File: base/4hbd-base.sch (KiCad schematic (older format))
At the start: 13 parts, among them J1 Screw_Terminal_01x03, J10 Screw_Terminal_01x04, J11 Screw_Terminal_01x02, J12 Conn_01x03, J13 Conn_01x08, J2 Screw_Terminal_01x03, J3 Screw_Terminal_01x03, J4 Screw_Terminal_01x03, J5 Screw_Terminal_01x02, J6 Screw_Terminal_01x02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

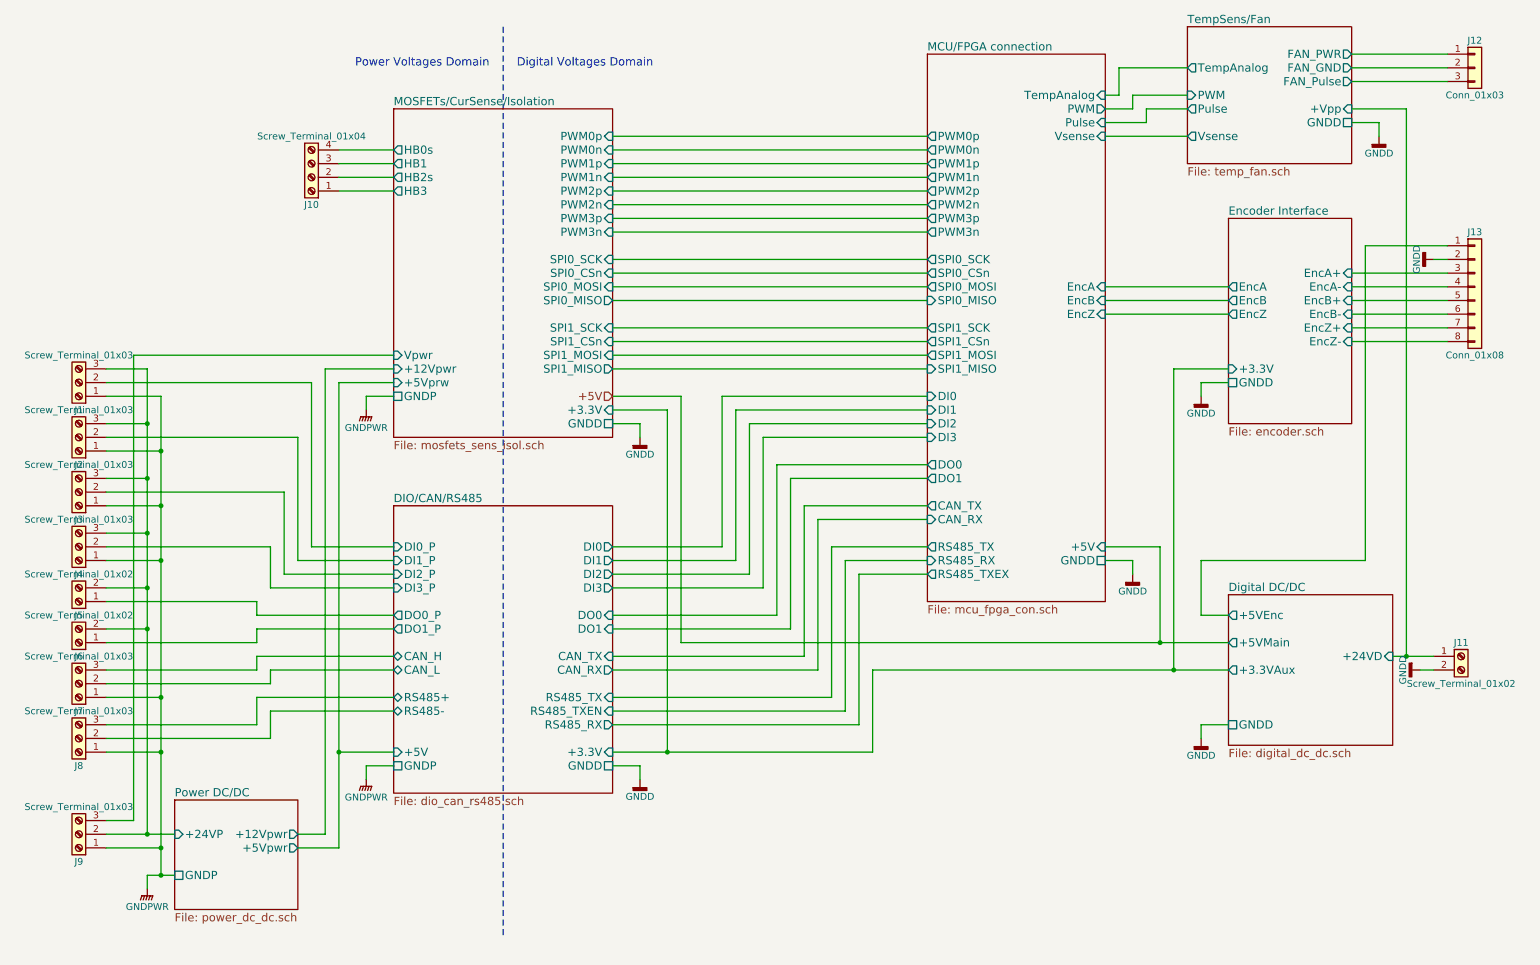
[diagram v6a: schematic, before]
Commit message: 1. Separate dio_can_rs485 sheet into two: dio + can_rs485. 2. Move can and rs485 into digital power domain 3. Add CAN transiever to can_rs485 sheet
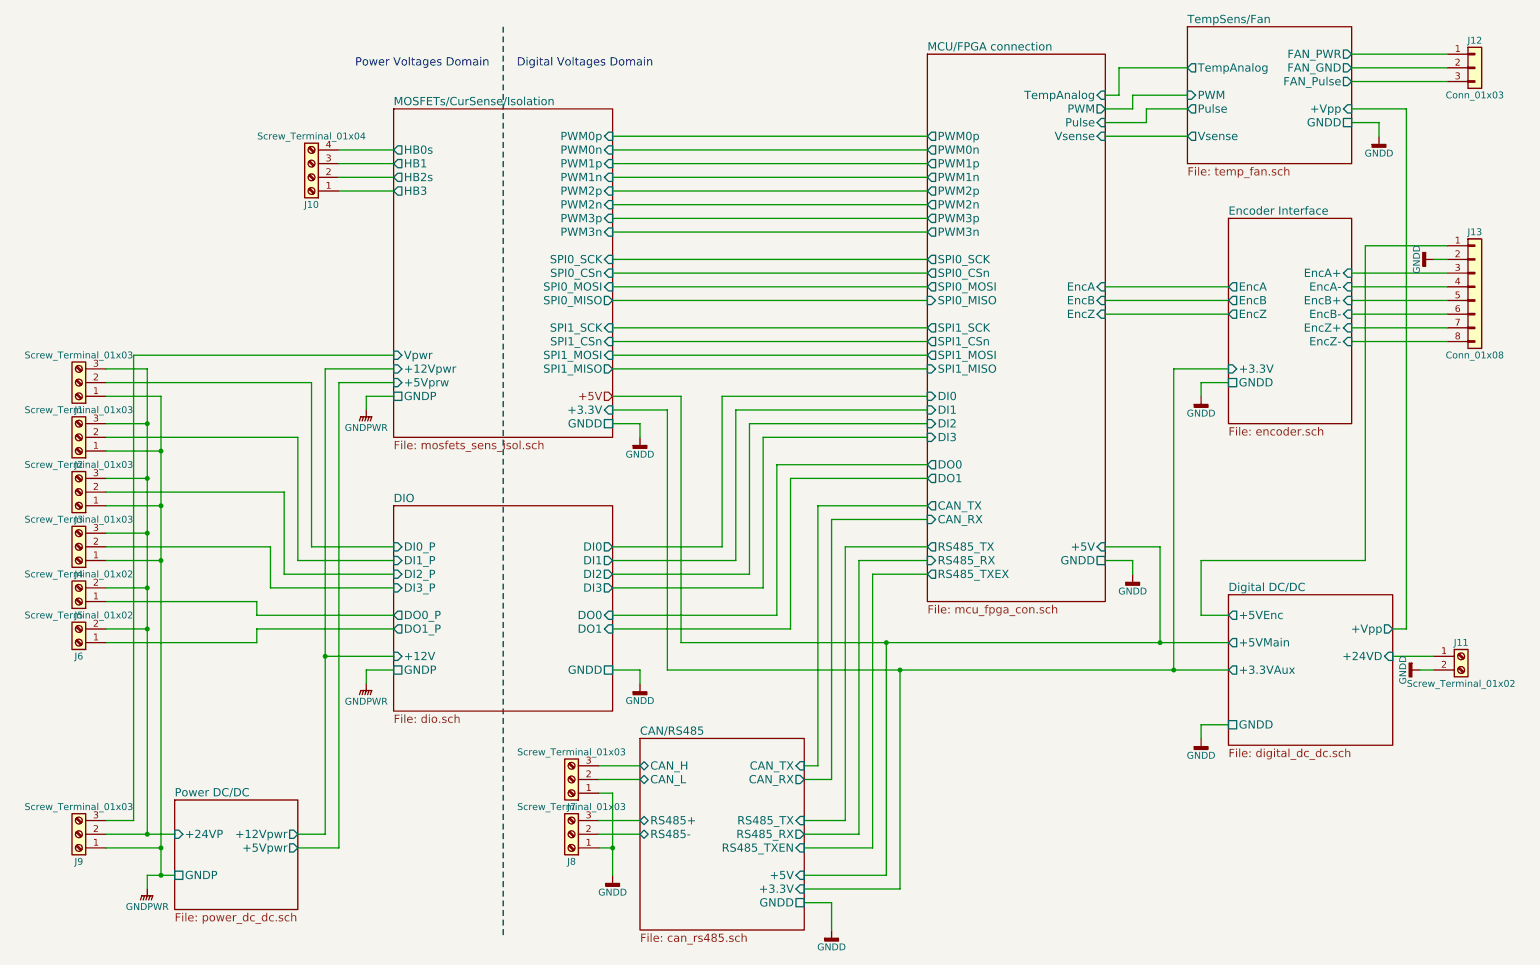
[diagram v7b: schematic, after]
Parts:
- J13: footprint (none) -> Connector_PinHeader_2.54mm:PinHeader_1x08_P2.54mm_Horizontal
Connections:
- net GNDD: now also J7.1 (Pin_1), J8.1 (Pin_1)
- net GNDPWR: no longer J7.1 (Pin_1), J8.1 (Pin_1)
- net DIO/CAN/RS485/CAN_H renamed CAN/RS485/CAN_H
- net DIO/CAN/RS485/CAN_L renamed CAN/RS485/CAN_L
- net DIO/CAN/RS485/DI0_P renamed DIO/DI0_P
- net DIO/CAN/RS485/DI1_P renamed DIO/DI1_P
- net DIO/CAN/RS485/DI2_P renamed DIO/DI2_P
- net DIO/CAN/RS485/DI3_P renamed DIO/DI3_P
- net DIO/CAN/RS485/DO0_P renamed DIO/DO0_P
- net DIO/CAN/RS485/DO1_P renamed DIO/DO1_P
- net DIO/CAN/RS485/RS485+ renamed CAN/RS485/RS485+
- net DIO/CAN/RS485/RS485- renamed CAN/RS485/RS485-
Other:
- moved on the sheet: J7, J8
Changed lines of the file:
@@
 LIBS:dc-dc
 LIBS:regul
+LIBS:interface
+LIBS:ESD_Protection
 LIBS:4hbd-base-cache
 EELAYER 25 0
@@
 $Descr A4 11693 8268
 encoding utf-8
-Sheet 1 8
+Sheet 1 9
 Title ""
 Date ""
@@
 $EndSheet
 $Sheet
-S 3000 4300 1600 2100
+S 3000 4300 1600 1500
 U 5A1BA75E
-F0 "DIO/CAN/RS485" 60
-F1 "dio_can_rs485.sch" 60
+F0 "DIO" 60
+F1 "dio.sch" 60
 F2 "DI0_P" I L 3000 4600 60
 F3 "DI1_P" I L 3000 4700 60
@@
 F6 "DO0_P" O L 3000 5100 60
 F7 "DO1_P" O L 3000 5200 60
-F8 "CAN_H" B L 3000 5400 60
-F9 "CAN_L" B L 3000 5500 60
-F10 "DI0" O R 4600 4600 60
-F11 "DI1" O R 4600 4700 60
-F12 "DI2" O R 4600 4800 60
-F13 "DI3" O R 4600 4900 60
-F14 "DO0" I R 4600 5100 60
-F15 "DO1" I R 4600 5200 60
-F16 "CAN_TX" I R 4600 5400 60
-F17 "CAN_RX" O R 4600 5500 60
-F18 "RS485_TX" I R 4600 5700 60
-F19 "RS485_TXEN" I R 4600 5800 60
-F20 "RS485_RX" O R 4600 5900 60
-F21 "RS485+" B L 3000 5700 60
-F22 "RS485-" B L 3000 5800 60
-F23 "+3.3V" I R 4600 6100 60
-F24 "GNDD" U R 4600 6200 60
-F25 "+5V" I L 3000 6100 60
-F26 "GNDP" U L 3000 6200 60
+F8 "DI0" O R 4600 4600 60
+F9 "DI1" O R 4600 4700 60
+F10 "DI2" O R 4600 4800 60
+F11 "DI3" O R 4600 4900 60
+F12 "DO0" I R 4600 5100 60
+F13 "DO1" I R 4600 5200 60
+F14 "GNDD" U R 4600 5500 60
+F15 "GNDP" U L 3000 5500 60
+F16 "+12V" I L 3000 5400 60
 $EndSheet
 Text Notes 3700 1100 2    60   ~ 0
@@
 F5 "+3.3VAux" O L 9100 5500 60
 F6 "GNDD" U L 9100 5900 60
+F7 "+Vpp" O R 10300 5200 60
 $EndSheet
 $Sheet
@@
 L GNDD #PWR5
 U 1 1 5A1C5445
-P 4800 6300
-F 0 "#PWR5" H 4800 6050 50  0001 C CNN
-F 1 "GNDD" H 4800 6175 50  0000 C CNN
-F 2 "" H 4800 6300 50  0001 C CNN
-F 3 "" H 4800 6300 50  0001 C CNN
-	1    4800 6300
+P 4800 5600
+F 0 "#PWR5" H 4800 5350 50  0001 C CNN
+F 1 "GNDD" H 4800 5475 50  0000 C CNN
+F 2 "" H 4800 5600 50  0001 C CNN
+F 3 "" H 4800 5600 50  0001 C CNN
+	1    4800 5600
 	1    0    0    -1
 $EndComp
@@
 F 0 "J13" H 10900 3100 50  0000 C CNN
 F 1 "Conn_01x08" H 10900 2200 50  0000 C CNN
-F 2 "" H 10900 2700 50  0001 C CNN
+F 2 "Connector_PinHeader_2.54mm:PinHeader_1x08_P2.54mm_Horizontal" H 10900 2700 50  0001 C CNN
 F 3 "" H 10900 2700 50  0001 C CNN
 	1    10900 2700
@@
 	8900 3400 8900 3500
 Wire Wire Line
-	4600 6200 4800 6200
-Wire Wire Line
-	4800 6200 4800 6300
+	4600 5500 4800 5500
+Wire Wire Line
+	4800 5500 4800 5600
 Wire Wire Line
 	4600 3700 4800 3700
@@
 	5900 5200 4600 5200
 Wire Wire Line
-	4600 5400 6000 5400
-Wire Wire Line
-	6000 5400 6000 4300
-Wire Wire Line
-	6100 4400 6100 5500
-Wire Wire Line
-	6100 5500 4600 5500
-Wire Wire Line
-	4600 5700 6200 5700
-Wire Wire Line
-	6200 5700 6200 4600
-Wire Wire Line
-	6300 4700 6300 5800
-Wire Wire Line
-	6300 5800 4600 5800
-Wire Wire Line
-	4600 5900 6400 5900
-Wire Wire Line
-	6400 5900 6400 4800
-Wire Wire Line
-	6500 6100 6500 5500
-Wire Wire Line
-	4600 6100 6500 6100
-Wire Wire Line
 	4600 3600 5000 3600
-Wire Wire Line
-	5000 3600 5000 6100
-Connection ~ 5000 6100
 Wire Wire Line
 	8700 5500 8700 3300
@@
 	5900 4100 6900 4100
 Wire Wire Line
-	6500 5500 9100 5500
-Wire Wire Line
-	6000 4300 6900 4300
-Wire Wire Line
-	6100 4400 6900 4400
-Wire Wire Line
-	6200 4600 6900 4600
-Wire Wire Line
-	6300 4700 6900 4700
-Wire Wire Line
-	6400 4800 6900 4800
+	5000 5500 9100 5500
 Wire Wire Line
 	4600 2800 6900 2800
@@
 	8900 4700 10100 4700
 Wire Wire Line
-	10400 1400 10400 5400
-Wire Wire Line
 	10400 1400 10000 1400
-Connection ~ 10400 5400
 $Comp
 L Conn_01x03 J12
@@
 	2800 3500 2800 3600
 Wire Wire Line
-	3000 6200 2800 6200
-Wire Wire Line
-	2800 6200 2800 6300
+	3000 5500 2800 5500
+Wire Wire Line
+	2800 5500 2800 5600
 Wire Wire Line
 	1200 7000 1400 7000
@@
 L GNDPWR #PWR3
 U 1 1 5A1F43A1
-P 2800 6300
-F 0 "#PWR3" H 2800 6100 50  0001 C CNN
-F 1 "GNDPWR" H 2800 6170 50  0000 C CNN
-F 2 "" H 2800 6250 50  0001 C CNN
-F 3 "" H 2800 6250 50  0001 C CNN
-	1    2800 6300
+P 2800 5600
+F 0 "#PWR3" H 2800 5400 50  0001 C CNN
+F 1 "GNDPWR" H 2800 5470 50  0000 C CNN
+F 2 "" H 2800 5550 50  0001 C CNN
+F 3 "" H 2800 5550 50  0001 C CNN
+	1    2800 5600
 	1    0    0    -1
 $EndComp
@@
 	2600 3400 2600 6800
 Wire Wire Line
-	2600 6100 3000 6100
-Wire Wire Line
 	2600 3400 3000 3400
-Connection ~ 2600 6100
 Wire Wire Line
 	2300 6700 2500 6700
@@
 L Screw_Terminal_01x03 J8
 U 1 1 5A1F99A1
-P 700 6000
-F 0 "J8" H 700 6200 50  0000 C CNN
-F 1 "Screw_Terminal_01x03" H 700 5800 50  0000 C CNN
-F 2 "" H 700 6000 50  0001 C CNN
-F 3 "" H 700 6000 50  0001 C CNN
-	1    700  6000
+P 4300 6700
+F 0 "J8" H 4300 6900 50  0000 C CNN
+F 1 "Screw_Terminal_01x03" H 4300 6500 50  0000 C CNN
+F 2 "" H 4300 6700 50  0001 C CNN
+F 3 "" H 4300 6700 50  0001 C CNN
+	1    4300 6700
 	-1   0    0    1
 $EndComp
@@
 L Screw_Terminal_01x03 J7
 U 1 1 5A1F9CC3
-P 700 5600
-F 0 "J7" H 700 5800 50  0000 C CNN
-F 1 "Screw_Terminal_01x03" H 700 5400 50  0000 C CNN
-F 2 "" H 700 5600 50  0001 C CNN
-F 3 "" H 700 5600 50  0001 C CNN
-	1    700  5600
+P 4300 6300
+F 0 "J7" H 4300 6500 50  0000 C CNN
+F 1 "Screw_Terminal_01x03" H 4300 6100 50  0000 C CNN
+F 2 "" H 4300 6300 50  0001 C CNN
+F 3 "" H 4300 6300 50  0001 C CNN
+	1    4300 6300
 	-1   0    0    1
 $EndComp
@@
 	1300 3500 1300 7000
 Connection ~ 1300 7000
-Wire Wire Line
-	1300 6100 900  6100
 Connection ~ 1300 6800
-Wire Wire Line
-	1300 5700 900  5700
-Connection ~ 1300 6100
 Wire Wire Line
 	1200 3300 1200 6700
@@
 Wire Wire Line
 	1300 4700 900  4700
-Connection ~ 1300 5700
 Wire Wire Line
 	1300 4300 900  4300
@@
 Wire Wire Line
 	2000 5300 900  5300
-Wire Wire Line
-	3000 5400 2000 5400
-Wire Wire Line
-	2000 5400 2000 5500
-Wire Wire Line
-	2000 5500 900  5500
-Wire Wire Line
-	3000 5500 2100 5500
-Wire Wire Line
-	2100 5500 2100 5600
-Wire Wire Line
-	2100 5600 900  5600
-Wire Wire Line
-	3000 5700 2000 5700
-Wire Wire Line
-	2000 5700 2000 5900
-Wire Wire Line
-	2000 5900 900  5900
-Wire Wire Line
-	3000 5800 2100 5800
-Wire Wire Line
-	2100 5800 2100 6000
-Wire Wire Line
-	2100 6000 900  6000
 Wire Wire Line
 	5100 5300 5100 3500
@@
 Text HLabel 4600 3500 0    60   Input ~ 0
 +5V
+Wire Wire Line
+	3000 5400 2500 5400
+Connection ~ 2500 5400
+Wire Wire Line
+	5000 3600 5000 5500
+$Sheet
+S 4800 6000 1200 1400
+U 5A3AD102
+F0 "CAN/RS485" 60
+F1 "can_rs485.sch" 60
+F2 "CAN_H" B L 4800 6200 60
+F3 "CAN_L" B L 4800 6300 60
+F4 "RS485+" B L 4800 6600 60
+F5 "RS485-" B L 4800 6700 60
+F6 "CAN_TX" I R 6000 6200 60
+F7 "CAN_RX" O R 6000 6300 60
+F8 "RS485_TX" I R 6000 6600 60
+F9 "RS485_TXEN" I R 6000 6800 60
+F10 "RS485_RX" O R 6000 6700 60
+F11 "+3.3V" I R 6000 7100 60
+F12 "GNDD" U R 6000 7200 60
+F13 "+5V" I R 6000 7000 60
+$EndSheet
+Wire Wire Line
+	6100 4300 6900 4300
+Wire Wire Line
+	6200 4400 6900 4400
+Wire Wire Line
+	6300 4600 6900 4600
+Wire Wire Line
+	6400 4700 6900 4700
+Wire Wire Line
+	6100 4300 6100 6200
+Wire Wire Line
+	6100 6200 6000 6200
+Wire Wire Line
+	6200 4400 6200 6300
+Wire Wire Line
+	6200 6300 6000 6300
+Wire Wire Line
+	6300 4600 6300 6600
+Wire Wire Line
+	6300 6600 6000 6600
+Wire Wire Line
+	6400 4700 6400 6700
+Wire Wire Line
+	6400 6700 6000 6700
+Wire Wire Line
+	6900 4800 6500 4800
+Wire Wire Line
+	6500 4800 6500 6800
+Wire Wire Line
+	6500 6800 6000 6800
+Wire Wire Line
+	6600 5300 6600 7000
+Wire Wire Line
+	6600 7000 6000 7000
+Connection ~ 6600 5300
+Wire Wire Line
+	6700 5500 6700 7100
+Wire Wire Line
+	6700 7100 6000 7100
+Connection ~ 6700 5500
+Wire Wire Line
+	6000 7200 6200 7200
+Wire Wire Line
+	6200 7200 6200 7400
+$Comp
+L GNDD #PWR?
+U 1 1 5A3B40B0
+P 6200 7400
+F 0 "#PWR?" H 6200 7150 50  0001 C CNN
+F 1 "GNDD" H 6200 7275 50  0000 C CNN
+F 2 "" H 6200 7400 50  0001 C CNN
+F 3 "" H 6200 7400 50  0001 C CNN
+	1    6200 7400
+	1    0    0    -1
+$EndComp
+$Comp
+L GNDD #PWR?
+U 1 1 5A3B43A6
+P 4600 7000
+F 0 "#PWR?" H 4600 6750 50  0001 C CNN
+F 1 "GNDD" H 4600 6875 50  0000 C CNN
+F 2 "" H 4600 7000 50  0001 C CNN
+F 3 "" H 4600 7000 50  0001 C CNN
+	1    4600 7000
+	1    0    0    -1
+$EndComp
+Wire Wire Line
+	4800 6600 4500 6600
+Wire Wire Line
+	4500 6700 4800 6700
+Wire Wire Line
+	4500 6300 4800 6300
+Wire Wire Line
+	4500 6200 4800 6200
+Wire Wire Line
+	4500 6400 4600 6400
+Wire Wire Line
+	4600 6400 4600 7000
+Wire Wire Line
+	4500 6800 4600 6800
+Connection ~ 4600 6800
+Wire Wire Line
+	10300 5200 10400 5200
+Wire Wire Line
+	10400 5200 10400 1400
 $EndSCHEMATC
